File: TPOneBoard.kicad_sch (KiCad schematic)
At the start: 40 parts, among them J1 BH 1750 FVI, J2 BME/BMP280, J3 Conn_01x06_Pin, J4 Conn_01x02_Pin, J5 TP4056 Modul, J6 Screw_Terminal_01x02, Q2 UMH3N, SW4 Close for prog., SW5 Reset, U1 CD4051B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

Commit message: 1. Stufe
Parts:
- removed R10, R11, R12, R13, R14, R15: 10K, FootPrints_TPC:R_1206_HandSolder, symbol Device:R
- added J7, J8: Conn_01x04_Socket, Connector_PinSocket_2.54mm:PinSocket_1x04_P2.54mm_Vertical, symbol Connector:Conn_01x04_Socket
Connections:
- net 18650+: now also J7.1 (Pin_1), J7.3 (Pin_3), J8.1 (Pin_1), J8.3 (Pin_3)
- net 18650-: now also J7.2 (Pin_2), J7.4 (Pin_4), J8.2 (Pin_2), J8.4 (Pin_4)
- net GND: now also U1.1 (X4), U1.12 (X3), U1.15 (X2), U1.2 (X6), U1.4 (X7), U1.5 (X5)

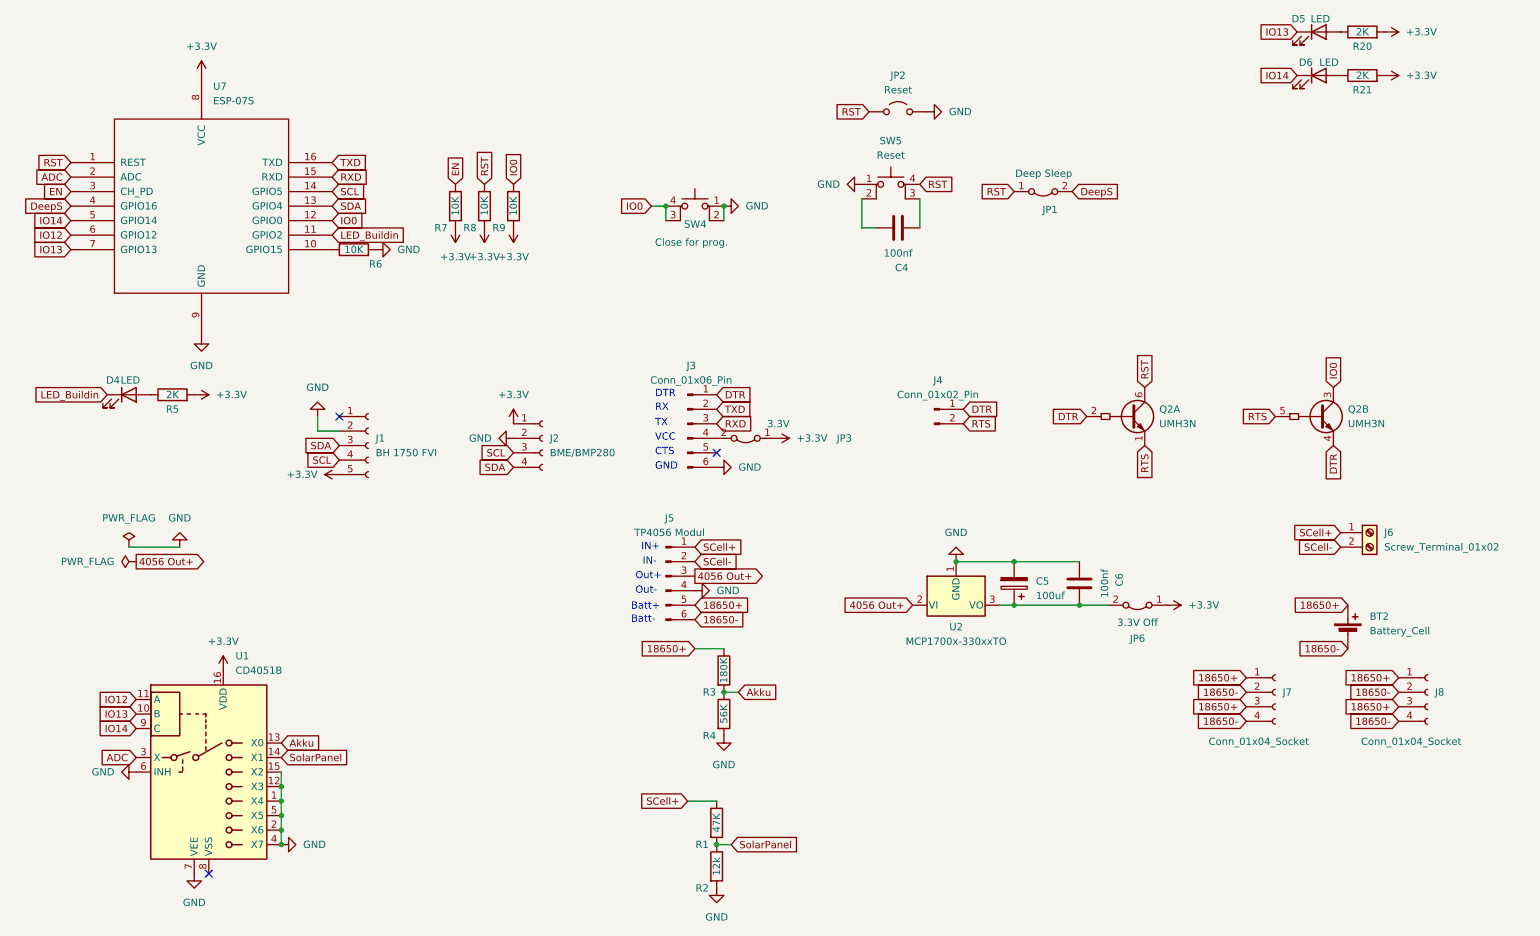
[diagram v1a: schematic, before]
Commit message: Platine Bestellt am 30.07.2025 Signed-off-by: TPComputerservice <78719315+TPComputerservice@users.noreply.github.com>
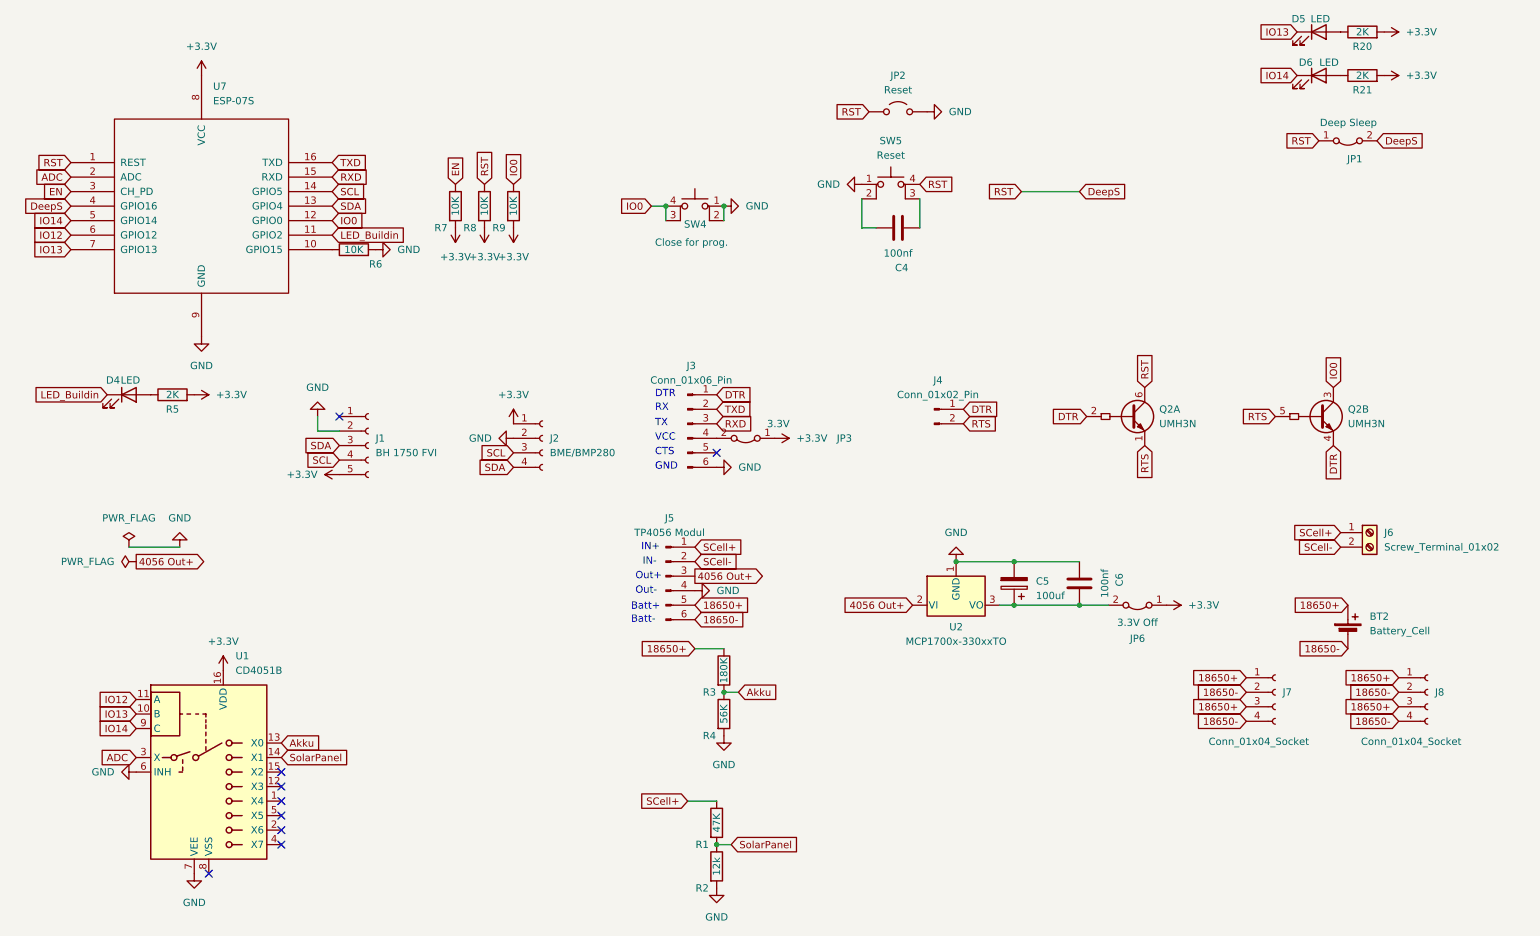
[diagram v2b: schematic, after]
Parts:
- J3: footprint Connector_PinHeader_2.54mm:PinHeader_1x06_P2.54mm_Vertical -> Connector_PinSocket_2.54mm:PinSocket_1x06_P2.54mm_Vertical
- U1: footprint Package_SO:SSOP-16_4.4x5.2mm_P0.65mm -> Package_SO:SO-16_3.9x9.9mm_P1.27mm
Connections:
- net RST is gone; now on net DeepS: JP1.1 (A), JP2.1 (A), Q2.6 (C1), R8.1, SW5.4 (A), U7.1 (REST)
- net GND: no longer U1.1 (X4), U1.12 (X3), U1.15 (X2), U1.2 (X6), U1.4 (X7), U1.5 (X5)
- no-connect marks 3 -> 9
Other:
- moved on the sheet: JP1
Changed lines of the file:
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@@
 	)
 	(junction
-		(at 64.77 154.94)
-		(diameter 0)
-		(color 0 0 0 0)
-	)
-	(junction
 		(at 140.97 160.02)
 		(diameter 0)
@@
 	)
 	(junction
-		(at 64.77 160.02)
-		(diameter 0)
-		(color 0 0 0 0)
-	)
-	(junction
 		(at 142.24 133.35)
 		(diameter 0)
@@
 	)
 	(junction
-		(at 64.77 152.4)
-		(diameter 0)
-		(color 0 0 0 0)
-	)
-	(junction
-		(at 64.77 149.86)
-		(diameter 0)
-		(color 0 0 0 0)
-	)
-	(junction
 		(at 193.04 118.11)
 		(diameter 0)
@@
 	)
 	(junction
-		(at 64.77 157.48)
-		(diameter 0)
-		(color 0 0 0 0)
-	)
-	(junction
 		(at 142.24 48.26)
 		(diameter 0)
@@
 	)
 	(no_connect
+		(at 64.77 147.32)
+	)
+	(no_connect
+		(at 64.77 149.86)
+	)
+	(no_connect
 		(at 52.07 165.1)
 	)
 	(no_connect
+		(at 64.77 157.48)
+	)
+	(no_connect
+		(at 64.77 152.4)
+	)
+	(no_connect
+		(at 64.77 154.94)
+	)
+	(no_connect
 		(at 74.93 85.09)
 	)
 	(no_connect
+		(at 64.77 160.02)
+	)
+	(no_connect
 		(at 140.97 91.44)
 	)
@@
 	(wire
 		(pts
-			(xy 132.08 48.26) (xy 132.08 50.8)
+			(xy 194.31 45.72) (xy 204.47 45.72)
 		)
 		(stroke
@@
 	(wire
 		(pts
-			(xy 64.77 157.48) (xy 64.77 160.02)
-		)
-		(stroke
-			(width 0)
-			(type default)
-		)
-	)
-	(wire
-		(pts
-			(xy 64.77 147.32) (xy 64.77 149.86)
+			(xy 132.08 48.26) (xy 132.08 50.8)
 		)
 		(stroke
@@
 	(wire
 		(pts
-			(xy 64.77 149.86) (xy 64.77 152.4)
-		)
-		(stroke
-			(width 0)
-			(type default)
-		)
-	)
-	(wire
-		(pts
 			(xy 142.24 133.35) (xy 144.78 133.35)
 		)
@@
 	(wire
 		(pts
-			(xy 64.77 154.94) (xy 64.77 157.48)
-		)
-		(stroke
-			(width 0)
-			(type default)
-		)
-	)
-	(wire
-		(pts
 			(xy 193.04 110.49) (xy 204.47 110.49)
 		)
@@
 	(wire
 		(pts
-			(xy 64.77 152.4) (xy 64.77 154.94)
-		)
-		(stroke
-			(width 0)
-			(type default)
-		)
-	)
-	(wire
-		(pts
 			(xy 38.1 107.95) (xy 46.99 107.95)
 		)
@@
 	(global_label "DeepS"
 		(shape input)
-		(at 203.2 45.72 0)
+		(at 256.54 36.83 0)
 		(fields_autoplaced yes)
 		(effects
@@
 		)
 		(property "Intersheetrefs" "${INTERSHEET_REFS}"
-			(at 211.3367 45.72 0)
+			(at 264.6767 36.83 0)
 			(effects
 				(font
@@
 		)
 	)
+	(global_label "RST"
+		(shape input)
+		(at 194.31 45.72 180)
+		(fields_autoplaced yes)
+		(effects
+			(font
+				(size 1.27 1.27)
+			)
+			(justify right)
+		)
+		(property "Intersheetrefs" "${INTERSHEET_REFS}"
+			(at 188.5387 45.7994 0)
+			(effects
+				(font
+					(size 1.27 1.27)
+				)
+				(justify left)
+				(hide yes)
+			)
+		)
+	)
 	(global_label "SCell+"
 		(shape input)
@@
 	(global_label "RST"
 		(shape input)
-		(at 193.04 45.72 180)
+		(at 246.38 36.83 180)
 		(fields_autoplaced yes)
 		(effects
@@
 		)
 		(property "Intersheetrefs" "${INTERSHEET_REFS}"
-			(at 187.2687 45.7994 0)
+			(at 240.6087 36.9094 0)
 			(effects
 				(font
@@
 		)
 	)
+	(global_label "DeepS"
+		(shape input)
+		(at 204.47 45.72 0)
+		(fields_autoplaced yes)
+		(effects
+			(font
+				(size 1.27 1.27)
+			)
+			(justify left)
+		)
+		(property "Intersheetrefs" "${INTERSHEET_REFS}"
+			(at 212.6067 45.72 0)
+			(effects
+				(font
+					(size 1.27 1.27)
+				)
+				(justify left)
+				(hide yes)
+			)
+		)
+	)
 	(global_label "18650-"
 		(shape input)
@@
 	(symbol
 		(lib_id "Jumper:Jumper_2_Bridged")
-		(at 198.12 45.72 0)
+		(at 251.46 36.83 0)
 		(mirror x)
 		(unit 1)
 		(exclude_from_sim no)
 		(in_bom yes)
-		(on_board yes)
+		(on_board no)
 		(dnp no)
 		(property "Reference" "JP1"
-			(at 200.66 48.895 0)
+			(at 254 40.005 0)
 			(effects
 				(font
@@
 		)
 		(property "Value" "Deep Sleep"
-			(at 203.2 42.545 0)
+			(at 256.54 33.655 0)
 			(effects
 				(font
@@
 		)
 		(property "Footprint" "Jumper:SolderJumper-2_P1.3mm_Bridged_RoundedPad1.0x1.5mm"
-			(at 198.12 45.72 0)
+			(at 251.46 36.83 0)
 			(effects
 				(font
@@
 		)
 		(property "Datasheet" "~"
-			(at 198.12 45.72 0)
+			(at 251.46 36.83 0)
 			(effects
 				(font
@@
 		)
 		(property "Description" ""
-			(at 198.12 45.72 0)
+			(at 251.46 36.83 0)
 			(effects
 				(font
@@
 			)
 		)
-		(property "Footprint" "Connector_PinHeader_2.54mm:PinHeader_1x06_P2.54mm_Vertical"
+		(property "Footprint" "Connector_PinSocket_2.54mm:PinSocket_1x06_P2.54mm_Vertical"
 			(at 135.89 86.36 0)
 			(effects
@@
 			)
 		)
-		(property "Footprint" "Package_SO:SSOP-16_4.4x5.2mm_P0.65mm"
+		(property "Footprint" "Package_SO:SO-16_3.9x9.9mm_P1.27mm"
 			(at 55.88 166.37 0)
 			(effects
@@
 					(unit 1)
 				)
-			)
-		)
-	)
-	(symbol
-		(lib_name "GND_1")
-		(lib_id "power:GND")
-		(at 64.77 160.02 90)
-		(unit 1)
-		(exclude_from_sim no)
-		(in_bom yes)
-		(on_board yes)
-		(dnp no)
-		(fields_autoplaced yes)
-		(property "Reference" "#PWR01"
-			(at 71.12 160.02 0)
-			(effects
-				(font
-					(size 1.27 1.27)
-				)
-				(hide yes)
-			)
-		)
-		(property "Value" "GND"
-			(at 68.58 160.0199 90)
-			(effects
-				(font
-					(size 1.27 1.27)
-				)
-				(justify right)
-			)
-		)
-		(property "Footprint" ""
-			(at 64.77 160.02 0)
-			(effects
-				(font
-					(size 1.27 1.27)
-				)
-				(hide yes)
-			)
-		)
-		(property "Datasheet" ""
-			(at 64.77 160.02 0)
-			(effects
-				(font
-					(size 1.27 1.27)
-				)
-				(hide yes)
-			)
-		)
-		(property "Description" "Power symbol creates a global label with name \"GND\" , ground"
-			(at 64.77 160.02 0)
-			(effects
-				(font
-					(size 1.27 1.27)
-				)
-				(hide yes)
-			)
-		)
-		(pin "1"
-		)
-		(instances
-			(project "TPOneBoard"
-				(path "/e63e39d7-6ac0-4ffd-8aa3-1841a4541b55"
-					(reference "#PWR01")
-					(unit 1)
-				)
